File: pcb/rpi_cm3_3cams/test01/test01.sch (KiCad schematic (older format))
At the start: 4 parts, among them U1 RaspberryPi-CM3+

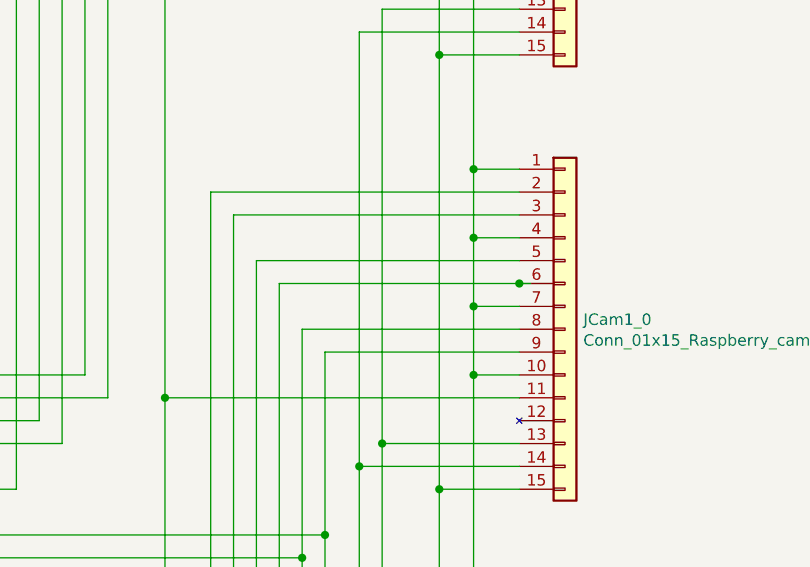
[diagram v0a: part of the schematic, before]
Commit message: kiCad/Rpi3cm_3cam: absolute path updated
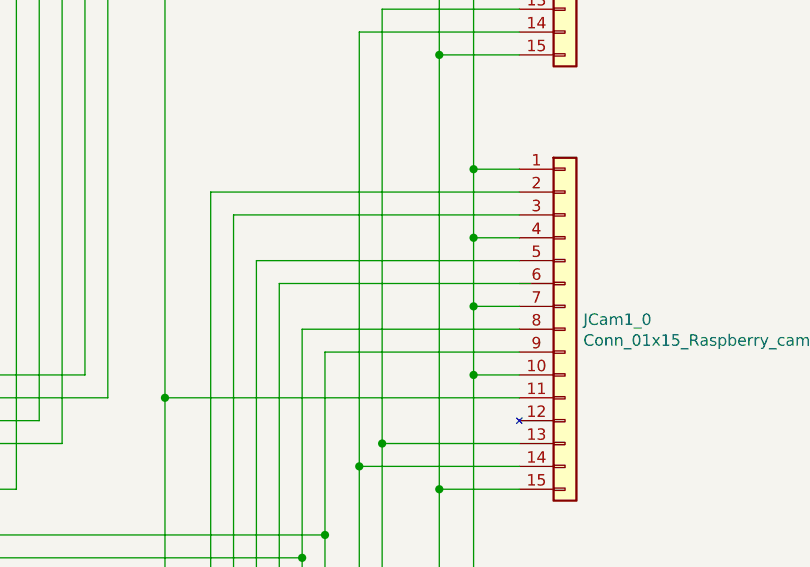
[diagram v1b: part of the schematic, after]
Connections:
- net at U1.153 (CAM1_DP1): no longer JCam1_0.6 (D1P)
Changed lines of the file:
@@
 Connection ~ 4900 5700
-Wire Wire Line
-	5900 4500 5850 4500
 Wire Wire Line
 	4800 4500 4800 6000
 Wire Wire Line
 	4800 6000 3300 6000
-Connection ~ 5850 4500
-Wire Wire Line
-	5850 4500 4800 4500
 Wire Wire Line
 	3300 6100 4700 6100
@@
 	800  7500 800  7600
 Connection ~ 2300 7500
+Wire Wire Line
+	4800 4500 5900 4500
 $EndSCHEMATC
